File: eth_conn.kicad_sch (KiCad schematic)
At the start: 27 parts, among them T1 H1102NLT

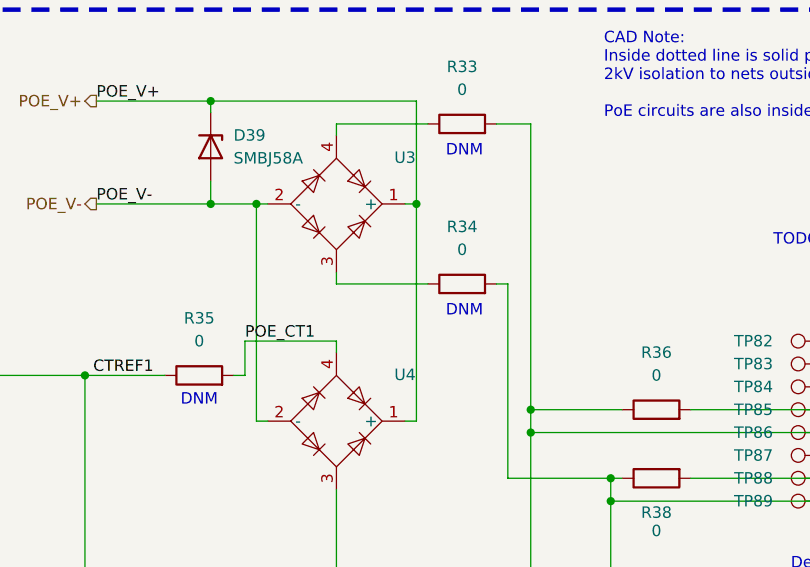
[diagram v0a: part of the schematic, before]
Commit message: did stuff, amongst others changed to op-amp input filter
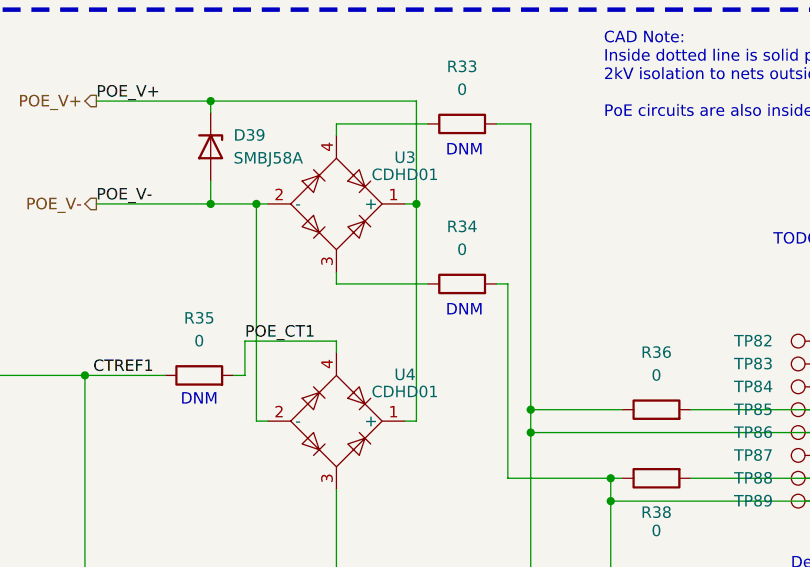
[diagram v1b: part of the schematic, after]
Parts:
- D39: LCSC (none) -> C157526
- RJ1: LCSC (none) -> C7501824
- T1: LCSC (none) -> C18584
- U3, U4: value (none) -> CDHD01

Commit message: did stuff
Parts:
- added U27: ESDS304DBVR, ESD304:DBV0005A_L, symbol ESD304:ESDS304DBVR
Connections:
- net GND: now also U27.2
- net MDI.RX+: now also U27.4
- net MDI.RX-: now also U27.5
- net MDI.TX+: now also U27.3
- net MDI.TX-: now also U27.1
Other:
- note removed: "TODO: add ESD"

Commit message: did stuff
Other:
- moved on the sheet: C36
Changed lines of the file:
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@@
 	)
 	(junction
-		(at 215.9 181.61)
+		(at 215.9 196.85)
 		(diameter 0)
 		(color 0 0 0 0)
@@
 	)
 	(junction
-		(at 265.43 181.61)
+		(at 265.43 196.85)
 		(diameter 0)
 		(color 0 0 0 0)
@@
 	)
 	(junction
-		(at 243.84 181.61)
+		(at 243.84 196.85)
 		(diameter 0)
 		(color 0 0 0 0)
@@
 	(wire
 		(pts
-			(xy 265.43 181.61) (xy 274.32 181.61)
+			(xy 265.43 196.85) (xy 274.32 196.85)
 		)
 		(stroke
@@
 	(wire
 		(pts
-			(xy 274.32 180.34) (xy 274.32 181.61)
+			(xy 274.32 180.34) (xy 274.32 196.85)
 		)
 		(stroke
@@
 	(wire
 		(pts
-			(xy 243.84 181.61) (xy 243.84 184.15)
+			(xy 243.84 196.85) (xy 243.84 199.39)
 		)
 		(stroke
@@
 	(wire
 		(pts
-			(xy 265.43 180.34) (xy 265.43 181.61)
+			(xy 265.43 180.34) (xy 265.43 196.85)
 		)
 		(stroke
@@
 	(wire
 		(pts
-			(xy 215.9 181.61) (xy 215.9 180.34)
+			(xy 215.9 196.85) (xy 215.9 180.34)
 		)
 		(stroke
@@
 	(wire
 		(pts
-			(xy 215.9 181.61) (xy 243.84 181.61)
+			(xy 215.9 196.85) (xy 243.84 196.85)
 		)
 		(stroke
@@
 	(wire
 		(pts
-			(xy 205.74 181.61) (xy 215.9 181.61)
+			(xy 205.74 196.85) (xy 215.9 196.85)
 		)
 		(stroke
@@
 	(wire
 		(pts
-			(xy 265.43 181.61) (xy 243.84 181.61)
+			(xy 265.43 196.85) (xy 243.84 196.85)
 		)
 		(stroke
@@
 	(wire
 		(pts
-			(xy 243.84 191.77) (xy 243.84 193.04)
+			(xy 243.84 207.01) (xy 243.84 208.28)
 		)
 		(stroke
@@
 	(wire
 		(pts
-			(xy 205.74 180.34) (xy 205.74 181.61)
+			(xy 205.74 180.34) (xy 205.74 196.85)
 		)
 		(stroke
@@
 	)
 	(label "MGND"
-		(at 233.68 181.61 0)
+		(at 233.68 196.85 0)
 		(effects
 			(font
@@
 	(symbol
 		(lib_id "Device:C")
-		(at 243.84 187.96 0)
+		(at 243.84 203.2 0)
 		(unit 1)
 		(body_style 1)
@@
 		(fields_autoplaced yes)
 		(property "Reference" "C36"
-			(at 247.65 186.6899 0)
+			(at 247.65 201.9299 0)
 			(show_name no)
 			(do_not_autoplace no)
@@
 		)
 		(property "Value" "1n 2000V"
-			(at 247.65 189.2299 0)
+			(at 247.65 204.4699 0)
 			(show_name no)
 			(do_not_autoplace no)
@@
 		)
 		(property "Footprint" "Capacitor_SMD:C_1206_3216Metric"
-			(at 244.8052 191.77 0)
+			(at 244.8052 207.01 0)
 			(hide yes)
 			(show_name no)
@@
 		)
 		(property "Datasheet" ""
-			(at 243.84 187.96 0)
+			(at 243.84 203.2 0)
 			(hide yes)
 			(show_name no)
@@
 		)
 		(property "Description" "Unpolarized capacitor"
-			(at 243.84 187.96 0)
+			(at 243.84 203.2 0)
 			(hide yes)
 			(show_name no)
@@
 		)
 		(property "Sim.Type" ""
-			(at 243.84 187.96 0)
+			(at 243.84 203.2 0)
 			(hide yes)
 			(show_name no)
@@
 		)
 		(property "KLC_S3.3" ""
-			(at 243.84 187.96 0)
+			(at 243.84 203.2 0)
 			(hide yes)
 			(show_name no)
@@
 		)
 		(property "KLC_S4.1" ""
-			(at 243.84 187.96 0)
+			(at 243.84 203.2 0)
 			(hide yes)
 			(show_name no)
@@
 		)
 		(property "LCSC Basic/Pref" "x"
-			(at 243.84 187.96 0)
+			(at 243.84 203.2 0)
 			(hide yes)
 			(show_name no)
@@
 		)
 		(property "LCSC" "C9196"
-			(at 243.84 187.96 0)
+			(at 243.84 203.2 0)
 			(hide yes)
 			(show_name no)
@@
 		)
 		(property "LCSC Part" "C9196"
-			(at 243.84 187.96 0)
+			(at 243.84 203.2 0)
 			(hide yes)
 			(show_name no)
@@
 		)
 		(property "LCSC missing" ""
-			(at 243.84 187.96 0)
+			(at 243.84 203.2 0)
 			(hide yes)
 			(show_name no)
@@
 		)
 		(property "Tolerance" ""
-			(at 243.84 187.96 0)
+			(at 243.84 203.2 0)
 			(hide yes)
 			(show_name no)
@@
 	(symbol
 		(lib_id "power:GNDPWR")
-		(at 243.84 193.04 0)
+		(at 243.84 208.28 0)
 		(unit 1)
 		(body_style 1)
@@
 		(fields_autoplaced yes)
 		(property "Reference" "#PWR068"
-			(at 243.84 198.12 0)
+			(at 243.84 213.36 0)
 			(hide yes)
 			(show_name no)
@@
 		)
 		(property "Value" "ETH_SHIELD"
-			(at 243.713 196.85 0)
+			(at 243.713 212.09 0)
 			(show_name no)
 			(do_not_autoplace no)
@@
 		)
 		(property "Footprint" ""
-			(at 243.84 194.31 0)
+			(at 243.84 209.55 0)
 			(hide yes)
 			(show_name no)
@@
 		)
 		(property "Datasheet" ""
-			(at 243.84 194.31 0)
+			(at 243.84 209.55 0)
 			(hide yes)
 			(show_name no)
@@
 		)
 		(property "Description" "Power symbol creates a global label with name \"GNDPWR\" , global ground"
-			(at 243.84 193.04 0)
+			(at 243.84 208.28 0)
 			(hide yes)
 			(show_name no)
